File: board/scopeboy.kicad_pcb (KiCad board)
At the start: 2 copper layers, 52 x 71.5 mm, 49 parts, among them J1 USB_B_Micro, J2 Conn_02x26_Odd_Even, J3 Conn_02x26_Odd_Even, J4 SM03B-SRSS-TB, SW1 SW_Push, SW2 SW_Push, U1 RP2350_80QFN, U2 NCP1117-3.3_SOT223, U3 W25Q128JVS, U4 DNF, Y1 ABM8-272-T3

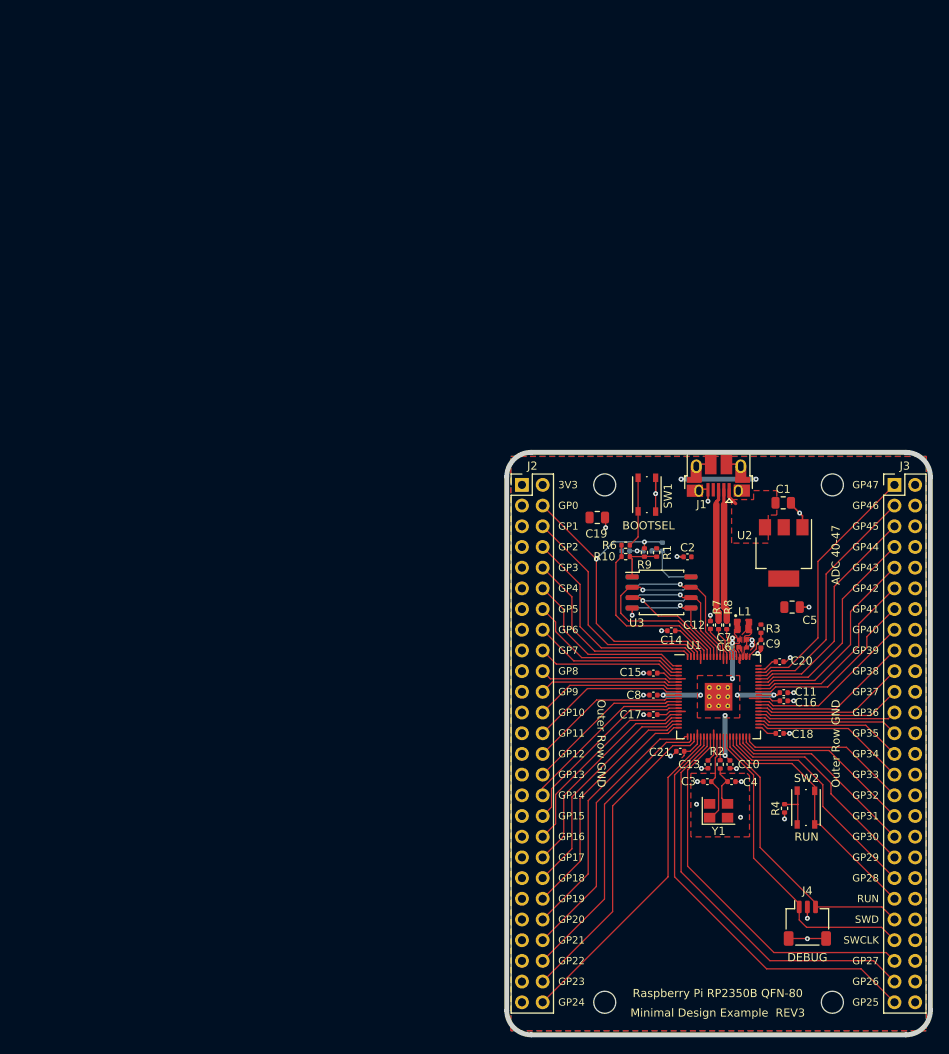
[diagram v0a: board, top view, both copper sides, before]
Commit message: All components in layout
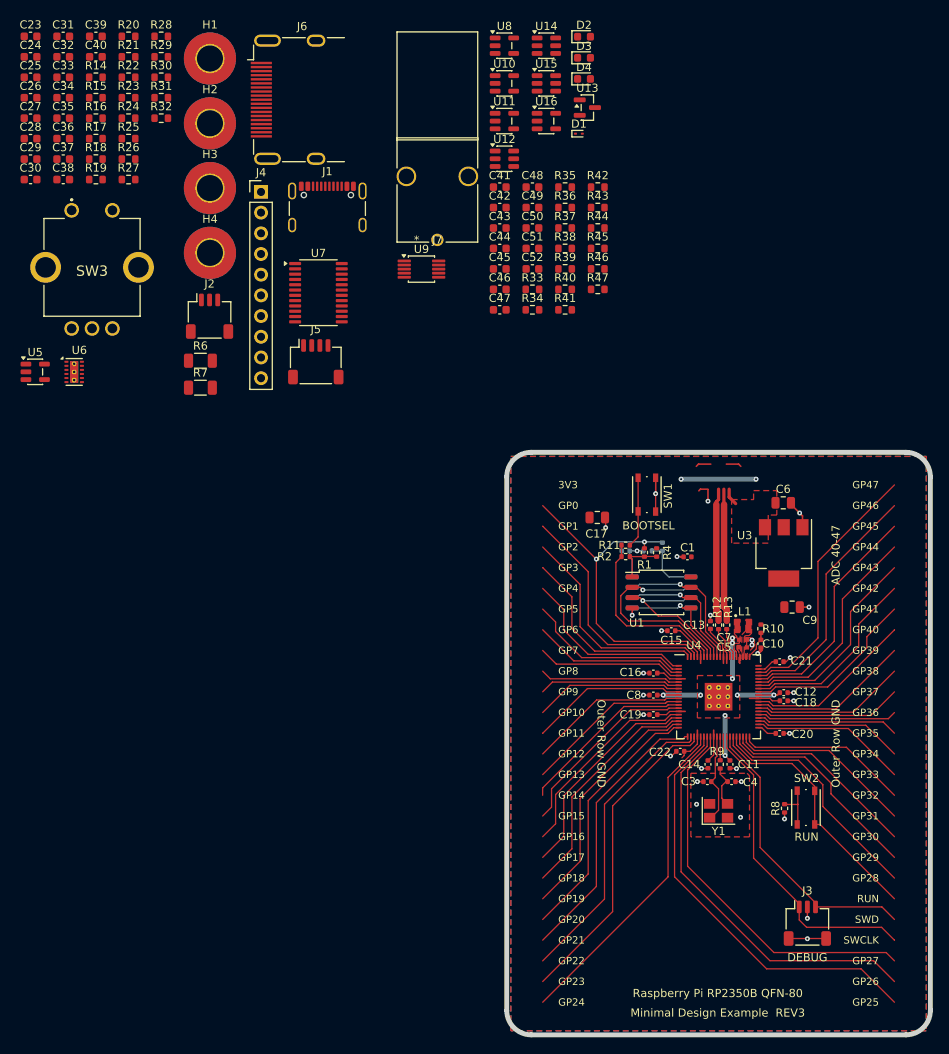
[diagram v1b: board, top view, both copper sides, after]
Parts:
- removed the J3 at (121.6, 74.0)
- added C23: 10nF, Capacitor_SMD:C_0603_1608Metric, F.Cu at (15.6, 18.9)
- added C24: 10nF, Capacitor_SMD:C_0603_1608Metric, F.Cu at (15.6, 21.5)
- added C25: 22u, Capacitor_SMD:C_0603_1608Metric, F.Cu at (15.6, 24.0)
- added C26: 2.2u, Capacitor_SMD:C_0603_1608Metric, F.Cu at (15.6, 26.5)
- added C27: 100n, Capacitor_SMD:C_0603_1608Metric, F.Cu at (15.6, 29.0)
- added C28: 22u, Capacitor_SMD:C_0603_1608Metric, F.Cu at (15.6, 31.5)
- added C29: 1u, Capacitor_SMD:C_0603_1608Metric, F.Cu at (15.6, 34.0)
- added C30: 2.2u, Capacitor_SMD:C_0603_1608Metric, F.Cu at (15.6, 36.5)
- added C31: 100n, Capacitor_SMD:C_0603_1608Metric, F.Cu at (19.6, 18.9)
- added C32: 100n, Capacitor_SMD:C_0603_1608Metric, F.Cu at (19.6, 21.5)
- added C33: 100n, Capacitor_SMD:C_0603_1608Metric, F.Cu at (19.6, 24.0)
- added C34: 10n, Capacitor_SMD:C_0603_1608Metric, F.Cu at (19.6, 26.5)
- added C35: 4.7u, Capacitor_SMD:C_0603_1608Metric, F.Cu at (19.6, 29.0)
- added C36: 100n, Capacitor_SMD:C_0603_1608Metric, F.Cu at (19.6, 31.5)
- added C37: 2.2u, Capacitor_SMD:C_0603_1608Metric, F.Cu at (19.6, 34.0)
- added C38: 22u, Capacitor_SMD:C_0603_1608Metric, F.Cu at (19.6, 36.5)
- added C39: 2.2u, Capacitor_SMD:C_0603_1608Metric, F.Cu at (23.6, 18.9)
- added C40: 2.2u, Capacitor_SMD:C_0603_1608Metric, F.Cu at (23.6, 21.5)
- added C41: 10pF, Capacitor_SMD:C_0603_1608Metric, F.Cu at (73.1, 37.5)
- added C42: 100n, Capacitor_SMD:C_0603_1608Metric, F.Cu at (73.1, 40.0)
- added C43: 100n, Capacitor_SMD:C_0603_1608Metric, F.Cu at (73.1, 42.5)
- added C44: 100n, Capacitor_SMD:C_0603_1608Metric, F.Cu at (73.1, 45.0)
- added C45: 100n, Capacitor_SMD:C_0603_1608Metric, F.Cu at (73.1, 47.5)
- added C46: 100n, Capacitor_SMD:C_0603_1608Metric, F.Cu at (73.1, 50.0)
- added C47: 120p, Capacitor_SMD:C_0603_1608Metric, F.Cu at (73.1, 52.5)
- added C48: 1u, Capacitor_SMD:C_0603_1608Metric, F.Cu at (77.2, 37.5)
- added C49: 100n, Capacitor_SMD:C_0603_1608Metric, F.Cu at (77.2, 40.0)
- added C50: 100n, Capacitor_SMD:C_0603_1608Metric, F.Cu at (77.2, 42.5)
- added C51: 100n, Capacitor_SMD:C_0603_1608Metric, F.Cu at (77.2, 45.0)
- added C52: 100n, Capacitor_SMD:C_0603_1608Metric, F.Cu at (77.2, 47.5)
- added D1: ESD9B5.0ST5G, Diode_SMD:D_SOD-923, F.Cu at (82.9, 30.9)
- added D2: BAT54WS-G3-08, Diode_SMD:D_0603_1608Metric, F.Cu at (83.5, 19.0)
- added D3: BAT54WS-G3-08, Diode_SMD:D_0603_1608Metric, F.Cu at (83.5, 21.6)
- added D4: D, Diode_SMD:D_0603_1608Metric, F.Cu at (83.5, 24.2)
- added J4: Conn_01x10, Connector_PinHeader_2.54mm:PinHeader_1x10_P2.54mm_Vertical, F.Cu at (43.8, 38.0)
- added J5: SM04B-SRSS-TB, Connector_JST:JST_SH_SM04B-SRSS-TB_1x04-1MP_P1.00mm_Horizontal, F.Cu at (50.6, 58.9)
- added J6: HDMI_A, Connector_Video:HDMI_A_Molex_208658-1001_Horizontal, F.Cu at (47.2, 26.7)
- added J7: 731000105, Footprints:CONN_73100-0105_MOL, F.Cu at (65.5, 43.9)
- added R14: 10K, Resistor_SMD:R_0603_1608Metric, F.Cu at (23.6, 24.0)
- added R15: 10K, Resistor_SMD:R_0603_1608Metric, F.Cu at (23.6, 26.5)
- added R16: 87k, Resistor_SMD:R_0603_1608Metric, F.Cu at (23.6, 29.0)
- added R17: 87k, Resistor_SMD:R_0603_1608Metric, F.Cu at (23.6, 31.5)
- added R18: 50k, Resistor_SMD:R_0603_1608Metric, F.Cu at (23.6, 34.0)
- added R19: 10K, Resistor_SMD:R_0603_1608Metric, F.Cu at (23.6, 36.5)
- added R20: 22, Resistor_SMD:R_0603_1608Metric, F.Cu at (27.6, 18.9)
- added R21: 50k, Resistor_SMD:R_0603_1608Metric, F.Cu at (27.6, 21.5)
- added R22: 0, Resistor_SMD:R_0603_1608Metric, F.Cu at (27.6, 24.0)
- added R23: 0, Resistor_SMD:R_0603_1608Metric, F.Cu at (27.6, 26.5)
- added R24: 220, Resistor_SMD:R_0603_1608Metric, F.Cu at (27.6, 29.0)
- added R25: 220, Resistor_SMD:R_0603_1608Metric, F.Cu at (27.6, 31.5)
- added R26: 220, Resistor_SMD:R_0603_1608Metric, F.Cu at (27.6, 34.0)
- added R27: 220, Resistor_SMD:R_0603_1608Metric, F.Cu at (27.6, 36.5)
- added R28: 220, Resistor_SMD:R_0603_1608Metric, F.Cu at (31.6, 18.9)
- added R29: 220, Resistor_SMD:R_0603_1608Metric, F.Cu at (31.6, 21.5)
- added R30: 220, Resistor_SMD:R_0603_1608Metric, F.Cu at (31.6, 24.0)
- added R31: 220, Resistor_SMD:R_0603_1608Metric, F.Cu at (31.6, 26.5)
- added R32: 10K, Resistor_SMD:R_0603_1608Metric, F.Cu at (31.6, 29.0)
- added R33: 100, Resistor_SMD:R_0603_1608Metric, F.Cu at (77.2, 50.0)
- added R34: 1M, Resistor_SMD:R_0603_1608Metric, F.Cu at (77.2, 52.5)
- added R35: 1k, Resistor_SMD:R_0603_1608Metric, F.Cu at (81.2, 37.5)
- added R36: 47, Resistor_SMD:R_0603_1608Metric, F.Cu at (81.2, 40.0)
- added R37: 100, Resistor_SMD:R_0603_1608Metric, F.Cu at (81.2, 42.5)
- added R38: 100, Resistor_SMD:R_0603_1608Metric, F.Cu at (81.2, 45.0)
- added R39: 680, Resistor_SMD:R_0603_1608Metric, F.Cu at (81.2, 47.5)
- added R40: 1k, Resistor_SMD:R_0603_1608Metric, F.Cu at (81.2, 50.0)
- added R41: 100, Resistor_SMD:R_0603_1608Metric, F.Cu at (81.2, 52.5)
- added R42: 100, Resistor_SMD:R_0603_1608Metric, F.Cu at (85.2, 37.5)
- added R43: 1k, Resistor_SMD:R_0603_1608Metric, F.Cu at (85.2, 40.0)
- added R44: 39, Resistor_SMD:R_0603_1608Metric, F.Cu at (85.2, 42.5)
- added R45: 1MEG, Resistor_SMD:R_0603_1608Metric, F.Cu at (85.2, 45.0)
- added R46: 1k, Resistor_SMD:R_0603_1608Metric, F.Cu at (85.2, 47.5)
- added R47: 22, Resistor_SMD:R_0603_1608Metric, F.Cu at (85.2, 50.0)
- added R6: 5.1k, Resistor_SMD:R_1206_3216Metric, F.Cu at (36.4, 58.8)
- added R7: 5.1k, Resistor_SMD:R_1206_3216Metric, F.Cu at (36.4, 62.1)
- added SW3: RotaryEncoder_Switch, Footprints:PEC11L4115FS0020, F.Cu at (20.6, 40.3)
- added U10: LMH6629, Package_TO_SOT_SMD:SOT-23-5, F.Cu at (73.7, 24.7)
- added U11: OPA820, Package_TO_SOT_SMD:SOT-23-5, F.Cu at (73.7, 29.3)
- added U12: DAC5571, Package_TO_SOT_SMD:SOT-23-6, F.Cu at (73.7, 34.0)
- added U13: LM4040DBZ-2.0, Package_TO_SOT_SMD:SOT-23, F.Cu at (83.9, 27.7)
- added U14: TLV3501, Package_TO_SOT_SMD:SOT-23-6, F.Cu at (78.9, 20.1)
- added U15: DAC5571, Package_TO_SOT_SMD:SOT-23-6, F.Cu at (78.9, 24.7)
- added U16: TLV9101, Package_TO_SOT_SMD:SOT-23-5, F.Cu at (78.9, 29.3)
- added U5: LP2985-3.3, Package_TO_SOT_SMD:SOT-23-5, F.Cu at (16.1, 60.1)
- added U6: LM27762, Package_SON:WSON-12-1EP_3x2mm_P0.5mm_EP1x2.65_ThermalVias, F.Cu at (20.9, 60.1)
- added U7: ADC08060, Package_SO:TSSOP-24_4.4x7.8mm_P0.65mm, F.Cu at (50.9, 50.4)
- added U8: OPA354, Package_TO_SOT_SMD:SOT-23-5, F.Cu at (73.7, 20.1)
- added U9: ADG621, Package_SO:MSOP-10_3x3mm_P0.5mm, F.Cu at (63.5, 47.5)
- H1, H2, H3, H4: footprint MountingHole:MountingHole_2.7mm_M2.5 -> MountingHole:MountingHole_3.2mm_M3_Pad_TopBottom
- J1: value USB_B_Micro -> USB_C_Receptacle_USB2.0_16P; footprint Connector_USB:USB_Micro-B_Amphenol_10103594-0001LF_Horizontal -> Connector_USB:USB_C_Receptacle_GCT_USB4105-xx-A_16P_TopMnt_Horizontal
- J2: value Conn_02x26_Odd_Even -> SM03B-SRSS-TB; footprint Connector_PinHeader_2.54mm:PinHeader_2x26_P2.54mm_Vertical -> Connector_JST:JST_SH_SM03B-SRSS-TB_1x03-1MP_P1.00mm_Horizontal
- moved H3 125.8 mm to (37.6, 37.6)
- moved H4 104.0 mm to (37.6, 45.5)
- moved H2 88.4 mm to (37.6, 29.6)
- moved H1 71.3 mm to (37.6, 21.7)
- moved J1 57.6 mm to (52.0, 41.0), turned to 0 degrees
- moved J2 43.6 mm to (37.5, 53.3)
- renumbered C2 to C1, C9 to C10, C10 to C11, C11 to C12, C12 to C13, C13 to C14, C14 to C15, C15 to C16, C19 to C17, C16 to C18, C17 to C19, C22 to C2, C18 to C20, C20 to C21, C21 to C22, C6 to C5, C1 to C6, C5 to C9, J4 to J3, R9 to R1, R3 to R10, R6 to R11, R7 to R12, R8 to R13, R10 to R2, R11 to R3, R1 to R4, R13 to R5, R4 to R8, R2 to R9, U3 to U1, U4 to U2, U2 to U3, U1 to U4
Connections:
- J2 pad 1: GND -> /RX
- J2 pad 2: +3V3 -> GND
- J2 pad 3: GND -> /TX
- U4 pad 11: /GPIO12 -> /D4
- U4 pad 12: /GPIO13 -> /D5
- U4 pad 13: /GPIO14 -> /D6
- U4 pad 14: /GPIO15 -> /D7
- U4 pad 20: /GPIO20 -> /SDA
- U4 pad 21: /GPIO21 -> /SCL
- U4 pad 23: /GPIO23 -> /ROTCLK
- U4 pad 25: /GPIO24 -> /ROTDT
- U4 pad 26: /GPIO25 -> /ROTSW
- U4 pad 36: /GPIO28 -> /TX
- U4 pad 37: /GPIO29 -> /RX
- U4 pad 6: /GPIO8 -> /D0
- U4 pad 7: /GPIO9 -> /D1
- U4 pad 77: /GPIO0 -> /MOSI
- U4 pad 78: /GPIO1 -> /LCDCS
- U4 pad 79: /GPIO2 -> /SCK
- U4 pad 8: /GPIO10 -> /D2
- U4 pad 80: /GPIO3 -> /MISO
- U4 pad 9: /GPIO11 -> /D3
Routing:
- net /ROTSW: track 0.00 -> 52.1 mm
- net /GPIO25: track 52.1 -> 0.00 mm
- net /ROTDT: track 0.00 -> 40.6 mm
- net /GPIO24: track 40.6 -> 0.00 mm
- net /ROTCLK: track 0.00 -> 39.0 mm
- net /GPIO23: track 39.0 -> 0.00 mm
- net /SCL: track 0.00 -> 34.2 mm
- net /GPIO21: track 34.2 -> 0.00 mm
- net /SDA: track 0.00 -> 31.7 mm
- net /GPIO20: track 31.7 -> 0.00 mm
- net /LCDCS: track 0.00 -> 29.4 mm
- net /GPIO1: track 29.4 -> 0.00 mm
- net /TX: track 0.00 -> 28.7 mm
- net /GPIO28: track 28.7 -> 0.00 mm
- net /SCK: track 0.00 -> 27.1 mm
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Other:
- copper layers 2 -> 4

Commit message: Positioned boards at same place
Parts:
- moved H1 216.5 mm to (215.7, 144.8)
- moved H3 181.9 mm to (215.7, 74.8)
- moved H2 145.0 mm to (125.7, 144.8)
- moved H4 92.8 mm to (125.7, 74.8)
- moved C11 63.4 mm to (47.4, 141.5)
- moved C9 63.4 mm to (55.0, 122.2)
- moved J3 63.4 mm to (56.9, 161.0)
- moved R1 63.4 mm to (36.9, 115.5)
- moved R4 63.4 mm to (38.4, 115.5)
- moved SW2 63.4 mm to (56.7, 146.8)
- moved C1 63.4 mm to (42.2, 116.0)
- moved C10 63.4 mm to (51.2, 126.7)
- moved C13 63.4 mm to (45.0, 124.4)
- moved C14 63.4 mm to (44.7, 141.5)
- moved C16 63.4 mm to (38.0, 130.3)
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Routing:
- net GND: track 38.8 -> 392.6 mm
- net /Analog Front End/CHASSIS: track 0.00 -> 226.4 mm
- net +3.3VA: track 0.00 -> 204.0 mm
- net VSYS: track 0.00 -> 167.1 mm
- net +3V3Pico: track 0.00 -> 163.0 mm
- net SDA: track 0.00 -> 147.2 mm
- net SCL: track 0.00 -> 146.3 mm
- net GNDA: track 0.00 -> 139.5 mm
- net Net-(J8-Pin_1): track 0.00 -> 137.9 mm
- net -3V3: track 0.00 -> 134.7 mm
- net SEL1: track 0.00 -> 131.2 mm
- net RX: track 0.00 -> 126.8 mm
- net TX: track 0.00 -> 121.7 mm
- net SEL0: track 0.00 -> 108.5 mm
- net ROTSW: track 0.00 -> 91.5 mm
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- added copper zone on In2.Cu, net +3V3
- added copper zone on In2.Cu, net -3V3
- added copper zone on In1.Cu, net GND
- added copper zone on B.Cu, net GNDA
- added copper zone on F.Cu, net GNDA
- added copper zone on In1.Cu, net GNDA
- added copper zone on In2.Cu, net VSYS
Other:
- board size 52 x 71.5 mm -> 200.7 x 104.8 mm

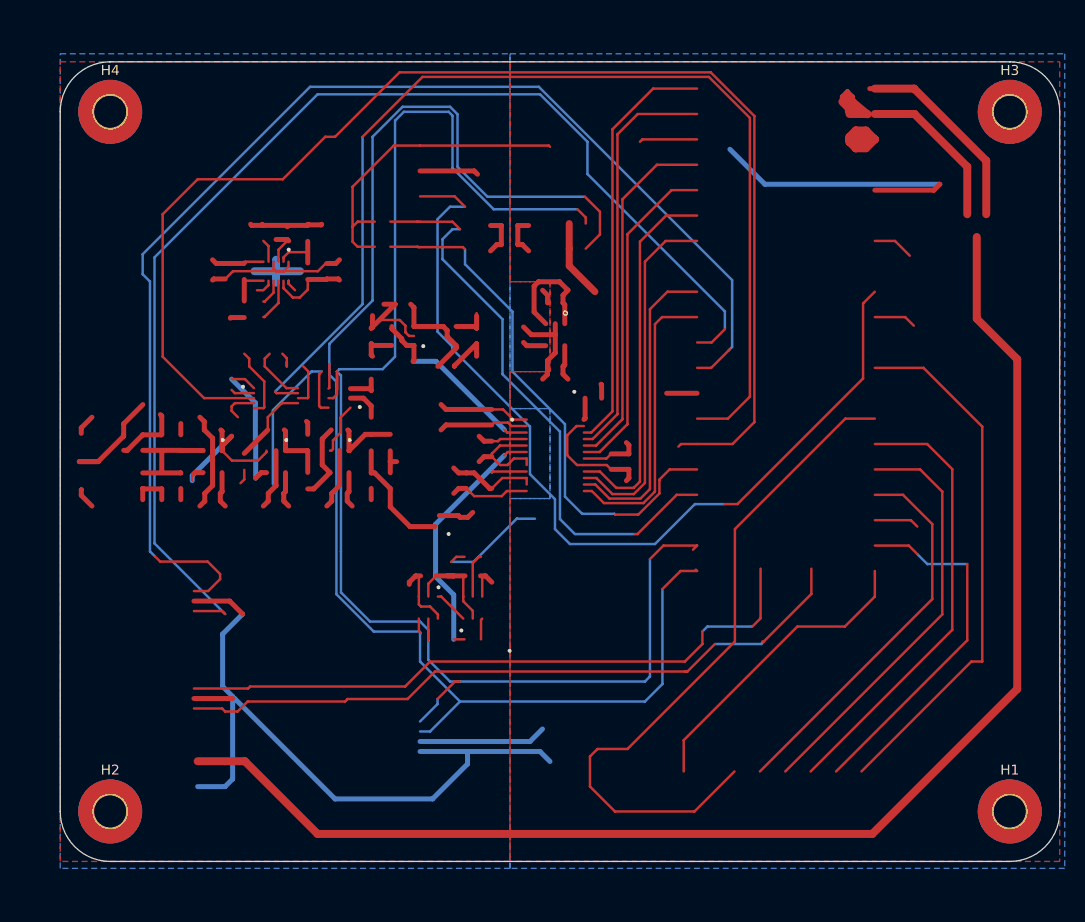
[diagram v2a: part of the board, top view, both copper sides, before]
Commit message: Replaced copper with vias
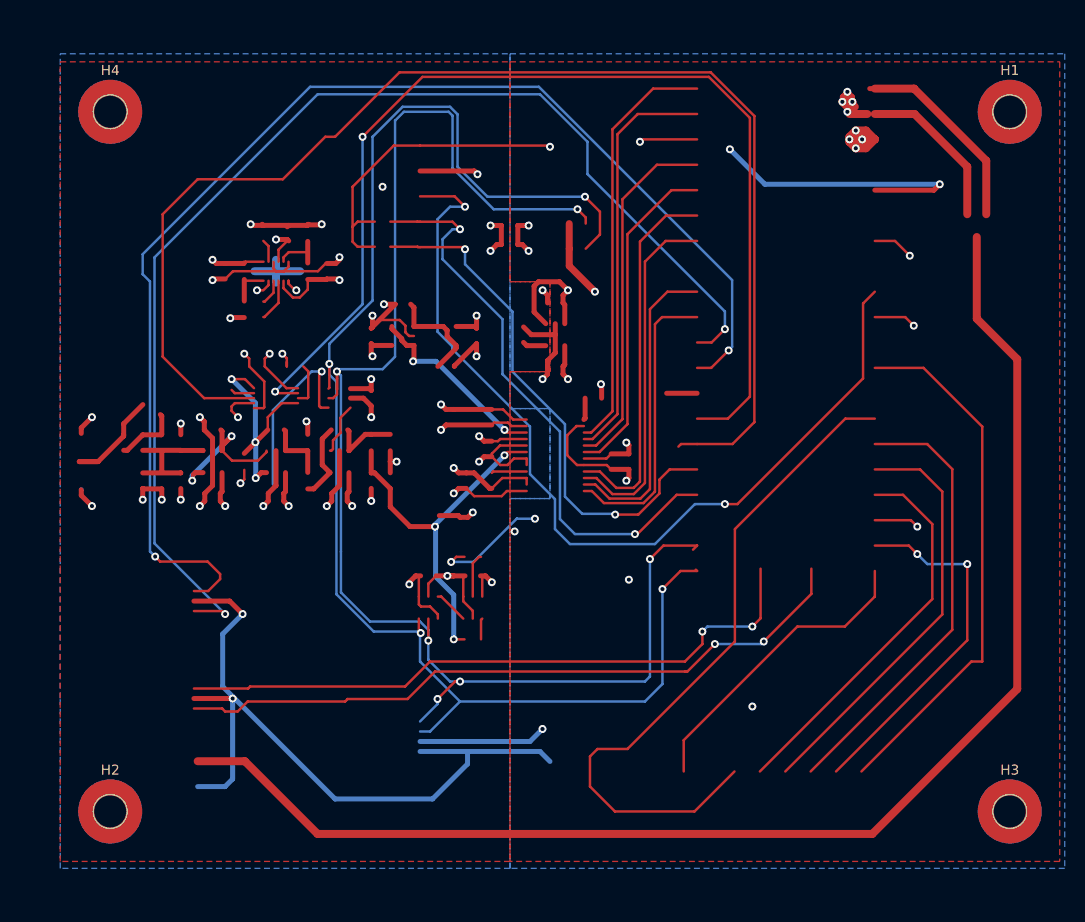
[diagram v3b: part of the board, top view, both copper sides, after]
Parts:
- moved H1 70.0 mm to (215.7, 74.8)
- moved H3 70.0 mm to (215.7, 144.8)
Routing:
- net GNDA: track 139.5 -> 365.9 mm, vias 0 -> 26
- net /Analog Front End/CHASSIS: track 226.4 -> 0.00 mm
- net Net-(J7-Pad1): track 12.0 -> 0.00 mm
- net Net-(D1-A): track 0.00 -> 12.0 mm
- net SDA: vias 0 -> 6
- net Net-(U3--): vias 0 -> 2
- net VSYS: vias 0 -> 8
- net VREF: vias 0 -> 2
- net VIN: vias 0 -> 3
- net TX: vias 0 -> 2
- net TRIG: vias 0 -> 3
- net SWIO: vias 0 -> 2
- net SWCLK: vias 0 -> 2
- net SEL0: vias 0 -> 2
- net SCL: vias 0 -> 4
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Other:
- board size 200.7 x 104.8 mm -> 52 x 71.5 mm

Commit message: Started placement
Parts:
- moved U7 133.0 mm to (170.2, 109.2)
- moved J2 117.6 mm to (131.7, 123.8), turned to -90 degrees
- moved D2 105.0 mm to (132.7, 111.8), turned to 90 degrees
- moved J3 80.0 mm to (132.0, 133.6), turned to -90 degrees
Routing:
- net RX: track 126.8 -> 0.00 mm, vias 2 -> 0
- net /RX: track 26.4 -> 153.2 mm, vias 0 -> 2
- net TX: track 121.7 -> 0.00 mm, vias 2 -> 0
- net /TX: track 28.7 -> 150.4 mm, vias 0 -> 2
- net SWIO: track 69.4 -> 0.00 mm, vias 2 -> 0
- net /SWD: track 35.6 -> 105.0 mm, vias 0 -> 2
- net /SWCLK: track 38.9 -> 104.2 mm, vias 0 -> 2
- net SWCLK: track 65.3 -> 0.00 mm, vias 2 -> 0
- net +3.3VA: track 204.0 -> 268.9 mm, vias 14 -> 20
- net -3V3: track 134.7 -> 69.8 mm, vias 9 -> 3
- net D0: track 42.1 -> 0.00 mm
- net /D0: track 17.2 -> 59.4 mm
- net D1: track 41.2 -> 0.00 mm
- net /D1: track 17.4 -> 58.6 mm
- net D4: track 37.4 -> 0.00 mm
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
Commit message: New merge placemetn
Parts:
- J5, SW3: moved to B.Cu
- moved U5 170.8 mm to (182.7, 98.2), turned to -90 degrees
- moved J4 169.0 mm to (177.9, 140.8), turned to 90 degrees
- moved C18 158.3 mm to (210.0, 106.5)
- moved C2 158.3 mm to (190.6, 88.0)
- moved R11 158.3 mm to (190.6, 87.3)
- moved R2 158.3 mm to (190.6, 88.8)
- moved R3 158.3 mm to (195.1, 87.5)
- moved R8 158.3 mm to (210.1, 119.7)
- moved SW2 158.3 mm to (212.7, 119.5)
- moved C1 158.3 mm to (198.1, 88.8)
- moved C10 158.3 mm to (207.2, 99.5)
- moved C11 158.3 mm to (203.3, 114.2)
- moved C12 158.3 mm to (209.9, 105.5)
- moved C13 158.3 mm to (200.9, 97.2)
- moved C14 158.3 mm to (200.7, 114.2)
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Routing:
- net GND: track 392.6 -> 26.4 mm, vias 46 -> 7
- net GNDA: track 365.9 -> 5.72 mm, vias 26 -> 0
- net +3.3VA: track 268.9 -> 0.00 mm, vias 20 -> 0
- net VSYS: track 167.1 -> 0.00 mm, vias 8 -> 0
- net +3V3Pico: track 163.0 -> 0.00 mm, vias 4 -> 0
- net /RX: track 153.2 -> 0.00 mm, vias 2 -> 0
- net /TX: track 150.4 -> 0.00 mm, vias 2 -> 0
- net SDA: track 147.2 -> 0.00 mm, vias 6 -> 0
- net SCL: track 146.3 -> 0.00 mm, vias 4 -> 0
- net Net-(J8-Pin_1): track 137.9 -> 0.00 mm
- net SEL1: track 131.2 -> 0.00 mm
- net SEL0: track 108.5 -> 0.00 mm, vias 2 -> 0
- net /SWD: track 105.0 -> 0.00 mm, vias 2 -> 0
- net /SWCLK: track 104.2 -> 0.00 mm, vias 2 -> 0
- net ROTSW: track 91.5 -> 0.00 mm, vias 2 -> 0
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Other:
- board size 52 x 71.5 mm -> 100 x 80 mm
- board text removed: "3V3"
- board text removed: "ADC 40-47"
- board text removed: "DEBUG"
- board text removed: "GP0"
- board text removed: "GP1"
- board text removed: "GP10"
- board text removed: "GP11"
- board text removed: "GP12"
- board text removed: "GP13"
- board text removed: "GP14"
- board text removed: "GP15"
- board text removed: "GP16"
- board text removed: "GP17"
- board text removed: "GP18"
- board text removed: "GP19"
- board text removed: "GP2"
- board text removed: "GP20"
- board text removed: "GP21"
- board text removed: "GP22"
- board text removed: "GP23"
- board text removed: "GP24"
- board text removed: "GP25"
- board text removed: "GP26"
- board text removed: "GP27"
- board text removed: "GP28"
- board text removed: "GP29"
- board text removed: "GP3"
- board text removed: "GP30"
- board text removed: "GP31"
- board text removed: "GP32"
- board text removed: "GP33"
- board text removed: "GP34"
- board text removed: "GP35"
- board text removed: "GP36"
- board text removed: "GP37"
- board text removed: "GP38"
- board text removed: "GP39"
- board text removed: "GP4"
- board text removed: "GP40"
- board text removed: "GP41"
- board text removed: "GP42"
- board text removed: "GP43"
- board text removed: "GP44"
- board text removed: "GP45"
- board text removed: "GP46"
- board text removed: "GP47"
- board text removed: "GP5"
- board text removed: "GP6"
- board text removed: "GP7"
- board text removed: "GP8"
- board text removed: "GP9"
- board text removed: "Minimal Design Example REV3"
- board text removed: "Outer Row GND"
- board text removed: "Raspberry Pi RP2350B QFN-80"
- board text removed: "SWCLK"
- board text removed: "SWD"
